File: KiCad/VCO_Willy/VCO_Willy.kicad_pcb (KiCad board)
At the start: 2 copper layers, 100 x 100 mm, 50 parts, among them J1 Conn_02x07_Odd_Even, J2 Conn_02x07_Odd_Even, J3 Conn_01x03_Male, J4 Conn_01x03_Male, J5 Conn_01x03_Male, U1 TL074, U2 TL074, U3 TL074

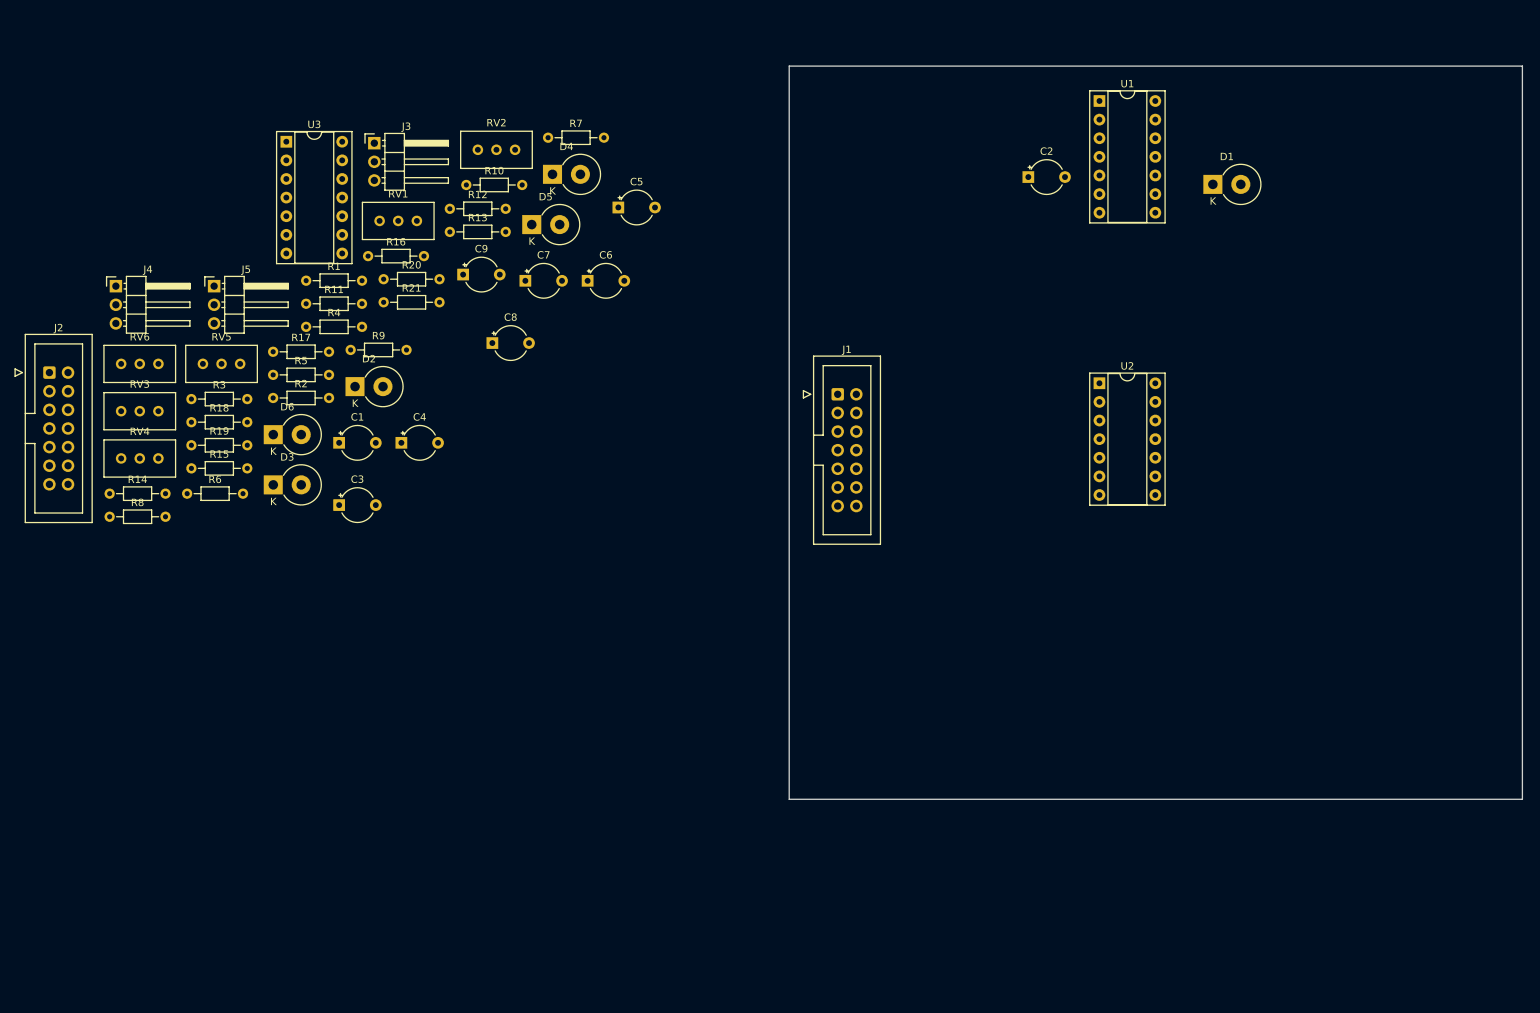
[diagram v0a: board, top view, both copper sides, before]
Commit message: Dämpfer,Filter,Peak implementiert auf PCB
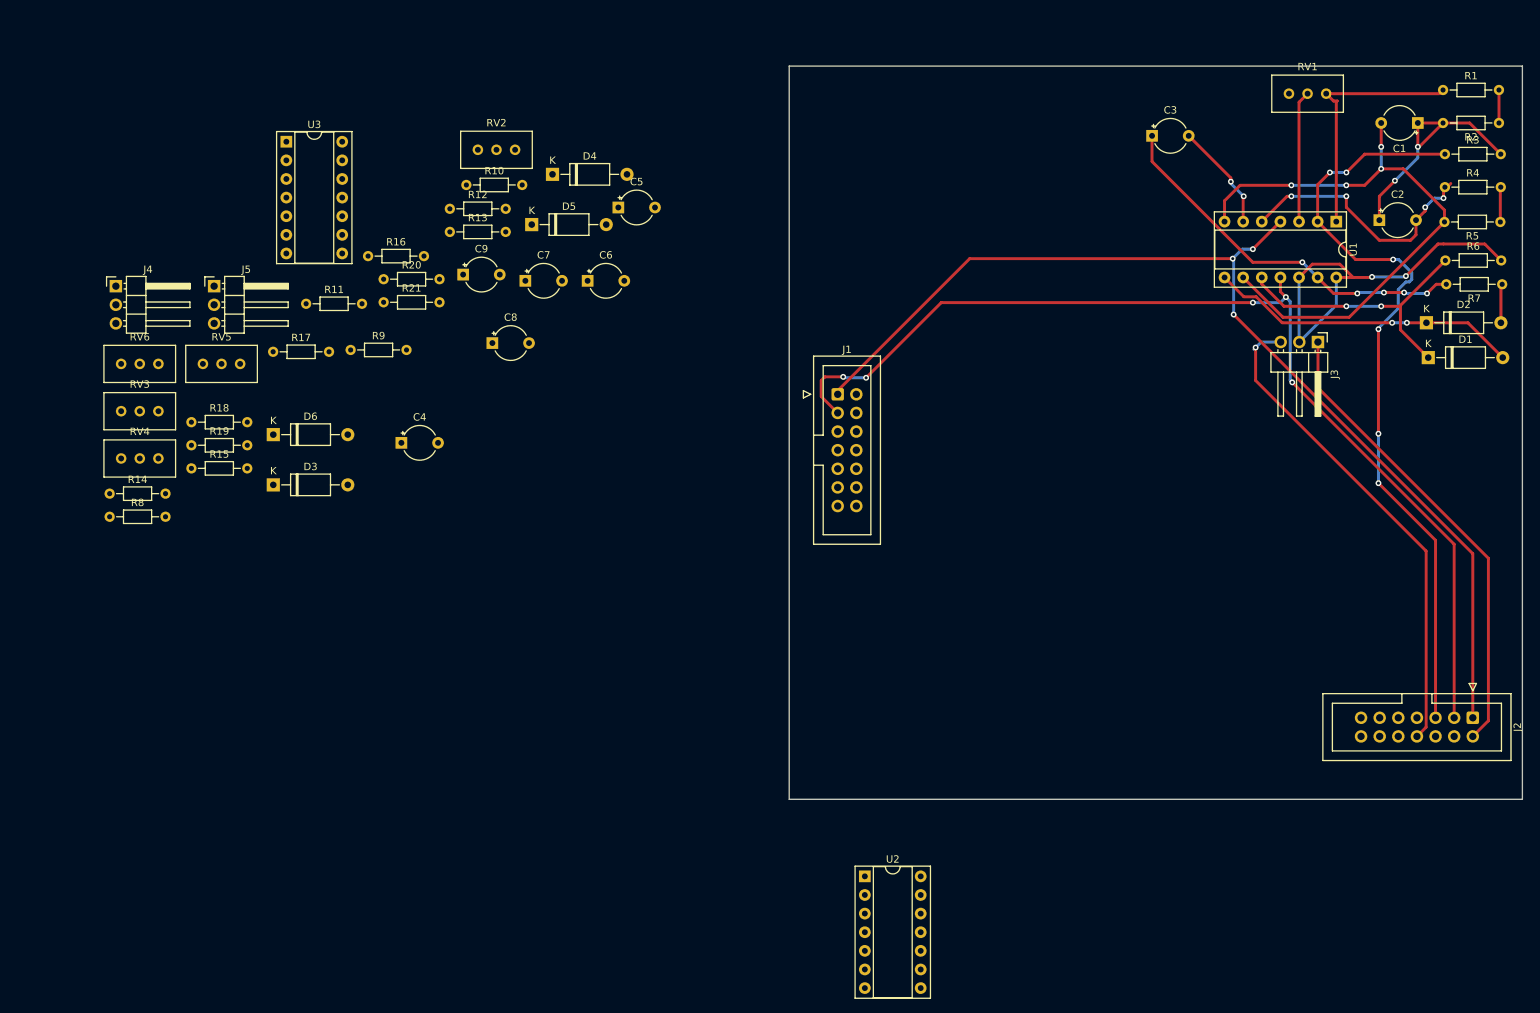
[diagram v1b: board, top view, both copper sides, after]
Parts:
- D1, D2, D3, D4, D5, D6: footprint Diode_THT:D_DO-201AE_P3.81mm_Vertical_KathodeUp -> Diode_THT:D_A-405_P10.16mm_Horizontal
- moved J2 199.8 mm to (229.6, 143.0), turned to -90 degrees
- moved R6 174.5 mm to (225.9, 80.6)
- moved R3 174.2 mm to (225.8, 66.1)
- moved R2 171.3 mm to (233.2, 61.9), turned to 180 degrees
- moved R5 168.7 mm to (233.4, 75.4), turned to 180 degrees
- moved R1 157.2 mm to (225.6, 57.4)
- moved R4 156.5 mm to (225.8, 70.6)
- moved C1 153.5 mm to (222.1, 61.9), turned to 180 degrees
- moved D2 146.4 mm to (223.3, 89.1)
- moved R7 131.7 mm to (233.6, 83.9), turned to 180 degrees
- moved J3 131.5 mm to (208.5, 91.8), turned to -90 degrees
- moved RV1 125.2 mm to (209.6, 57.9)
- moved C3 121.8 mm to (185.9, 63.6)
- moved U2 74.5 mm to (146.7, 164.6)
- moved C2 48.2 mm to (216.9, 75.1)
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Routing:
- net Net-(J1-Pad1): track 0.00 -> 146.6 mm, vias 0 -> 3
- net Net-(J1-Pad3): track 0.00 -> 143.6 mm, vias 0 -> 5
- net Net-(C3-Pad2): track 0.00 -> 120.8 mm, vias 0 -> 8
- net Net-(C1-Pad2): track 0.00 -> 79.9 mm, vias 0 -> 4
- net Net-(J2-Pad8): track 0.00 -> 67.3 mm, vias 0 -> 1
- net Net-(J2-Pad2): track 0.00 -> 64.3 mm
- net Net-(J3-Pad2): track 0.00 -> 54.1 mm, vias 0 -> 2
- net Net-(C3-Pad1): track 0.00 -> 51.7 mm, vias 0 -> 5
- net Net-(D1-Pad2): track 0.00 -> 42.5 mm, vias 0 -> 2
- net Net-(D1-Pad1): track 0.00 -> 38.5 mm, vias 0 -> 2
- net Net-(C2-Pad2): track 0.00 -> 36.0 mm, vias 0 -> 4
- net Net-(R1-Pad1): track 0.00 -> 34.6 mm
- net Net-(C1-Pad1): track 0.00 -> 33.5 mm, vias 0 -> 2
- net Net-(RV1-Pad2): track 0.00 -> 17.9 mm
- net Net-(D2-Pad2): track 0.00 -> 5.32 mm
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
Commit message: v3
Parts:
- moved RV3 178.7 mm to (228.6, 113.7), turned to 90 degrees
- moved R8 178.6 mm to (222.2, 111.8), turned to 180 degrees
- moved R14 151.8 mm to (194.9, 99.7), turned to -90 degrees
- moved R11 146.4 mm to (212.1, 123.8)
- moved R9 139.9 mm to (214.6, 115.6)
- moved D3 137.6 mm to (201.9, 89.5)
- moved RV4 134.1 mm to (183.5, 91.4)
- moved J4 131.8 mm to (163.2, 141.6)
- moved RV6 131.8 mm to (181.0, 112.4), turned to 180 degrees
- moved R10 130.0 mm to (212.7, 119.4)
- moved R18 129.7 mm to (181.0, 72.4), turned to 180 degrees
- moved R12 128.9 mm to (215.9, 101.6), turned to 180 degrees
- moved R19 121.7 mm to (173.4, 78.1)
- moved C4 116.3 mm to (199.4, 114.9)
- moved RV5 115.7 mm to (173.4, 65.4)
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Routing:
- net Net-(J1-Pad14): track 0.00 -> 280.6 mm, vias 0 -> 5
- net Net-(C3-Pad2): track 120.8 -> 390.2 mm, vias 8 -> 9
- net Net-(J1-Pad1): track 146.6 -> 341.3 mm, vias 3 -> 4
- net Net-(J4-Pad2): track 0.00 -> 139.3 mm, vias 0 -> 6
- net Net-(J2-Pad6): track 0.00 -> 133.9 mm
- net Net-(J3-Pad2): track 54.1 -> 181.2 mm, vias 2 -> 4
- net Net-(J5-Pad2): track 0.00 -> 111.9 mm, vias 0 -> 2
- net Net-(J2-Pad4): track 0.00 -> 110.7 mm
- net Net-(J2-Pad12): track 0.00 -> 91.1 mm, vias 0 -> 1
- net Net-(C6-Pad1): track 0.00 -> 78.5 mm
- net Net-(R15-Pad1): track 0.00 -> 75.5 mm, vias 0 -> 4
- net Net-(J2-Pad10): track 0.00 -> 71.6 mm, vias 0 -> 1
- net Net-(D1-Pad1): track 38.5 -> 107.0 mm, vias 2 -> 6
- net Net-(D5-Pad2): track 0.00 -> 67.6 mm, vias 0 -> 4
- net Net-(C4-Pad1): track 0.00 -> 67.2 mm
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
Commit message: upload new design
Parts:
- added REF**: MountingHole_3.2mm_M3, MountingHole:MountingHole_3.2mm_M3, F.Cu at (135.6, 57.4)
- added REF**: MountingHole_3.2mm_M3, MountingHole:MountingHole_3.2mm_M3, F.Cu at (194.7, 57.6)
- added REF**: MountingHole_3.2mm_M3, MountingHole:MountingHole_3.2mm_M3, F.Cu at (107.3, 146.3)
- D1, D2, D3, D4, D5, D6: footprint Diode_THT:D_A-405_P10.16mm_Horizontal -> Diode_THT:D_DO-35_SOD27_P7.62mm_Horizontal
- moved RV3 113.1 mm to (119.5, 84.0)
- moved R8 112.5 mm to (113.8, 81.7)
- moved R9 112.4 mm to (106.2, 85.9)
- moved R10 110.6 mm to (106.2, 89.6)
- moved U2 105.9 mm to (124.9, 83.0), turned to 0 degrees
- moved R12 101.7 mm to (114.3, 97.2), turned to 0 degrees
- moved R11 95.2 mm to (122.0, 93.1), turned to 180 degrees
- moved C5 93.0 mm to (106.9, 95.3)
- moved R18 86.5 mm to (122.3, 136.0)
- moved R19 85.6 mm to (114.9, 140.7)
- moved R2 83.8 mm to (150.5, 84.3), turned to 0 degrees
- moved C4 83.5 mm to (116.8, 102.5)
- moved RV5 81.2 mm to (119.8, 126.4), turned to 90 degrees
- moved C2 75.6 mm to (150.7, 93.2), turned to 0 degrees
- moved R1 75.6 mm to (158.1, 79.9)
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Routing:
- net Net-(J1-Pad3): track 175.5 -> 0.00 mm, vias 6 -> 0
- net Net-(J3-Pad2): track 181.2 -> 15.7 mm, vias 4 -> 0
- net Net-(J4-Pad2): track 139.3 -> 15.3 mm, vias 6 -> 0
- net Net-(D1-Pad1): track 107.0 -> 6.37 mm, vias 6 -> 0
- net Net-(J5-Pad2): track 111.9 -> 14.9 mm, vias 2 -> 0
- net Net-(J1-Pad1): track 341.3 -> 259.1 mm, vias 4 -> 5
- net Net-(C3-Pad2): track 390.2 -> 315.1 mm, vias 9 -> 4
- net Net-(R1-Pad1): track 81.5 -> 11.1 mm
- net Net-(J1-Pad14): track 280.6 -> 210.9 mm, vias 5 -> 4
- net Net-(R15-Pad1): track 75.5 -> 11.0 mm, vias 4 -> 0
- net Net-(J2-Pad6): track 133.9 -> 74.0 mm, vias 0 -> 2
- net Net-(D5-Pad2): track 67.6 -> 7.87 mm, vias 4 -> 0
- net Net-(D1-Pad2): track 60.6 -> 7.27 mm, vias 1 -> 0
- net Net-(C6-Pad1): track 78.5 -> 33.6 mm
- net Net-(RV5-Pad2): track 49.5 -> 6.07 mm, vias 2 -> 0
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- added copper zone on B.Cu, net Net-(J1-Pad3)
- added copper zone on F.Cu, net Net-(J1-Pad3)
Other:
- board text added: "Karim Nicolae Costan Moaiad Alsultan Max Genson TU Berlin Projektlabor WS 22/23 HexHex"
